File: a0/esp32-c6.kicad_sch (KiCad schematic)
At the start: 11 parts, among them J1 Conn_ARM_JTAG_SWD_10, SW1 SW_Push, SW2 SW_Push, U1 ESP32-C6-MINI-1/U

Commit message: update A0
Signed-off-by: Rodney Osodo <socials@rodneyosodo.com>
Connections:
- net USB_D+: now also U1.18 (GPIO13/USB_D+); no longer U1.17 (GPIO12/USB_D-)
- net USB_D-: now also U1.17 (GPIO12/USB_D-); no longer U1.18 (GPIO13/USB_D+)
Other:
- note added: "ESP32C6"
- note added: "JTAG"
- note added: "PULL UP"
- company: (none) -> Abstract Machines
- title: (none) -> A0
- moved on the sheet: C1, C2, C3, C4, J1, R1, R2, R3, SW1, SW2, U1

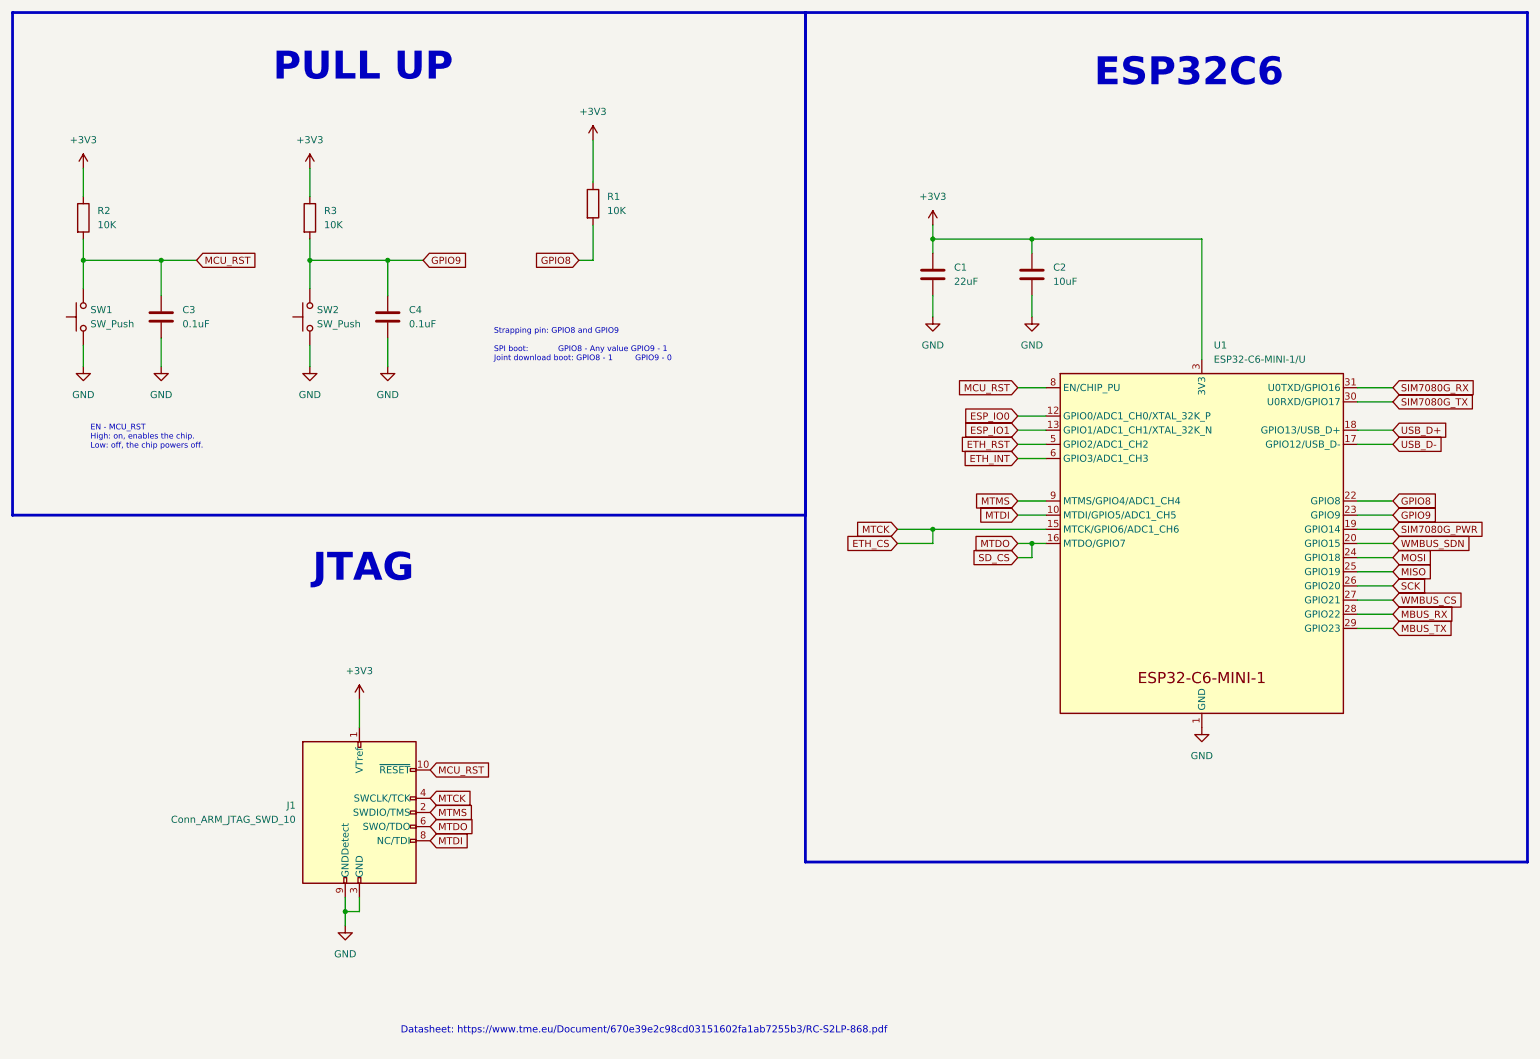
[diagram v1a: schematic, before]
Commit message: fix(A0): update to use modules
Signed-off-by: Rodney Osodo <socials@rodneyosodo.com>
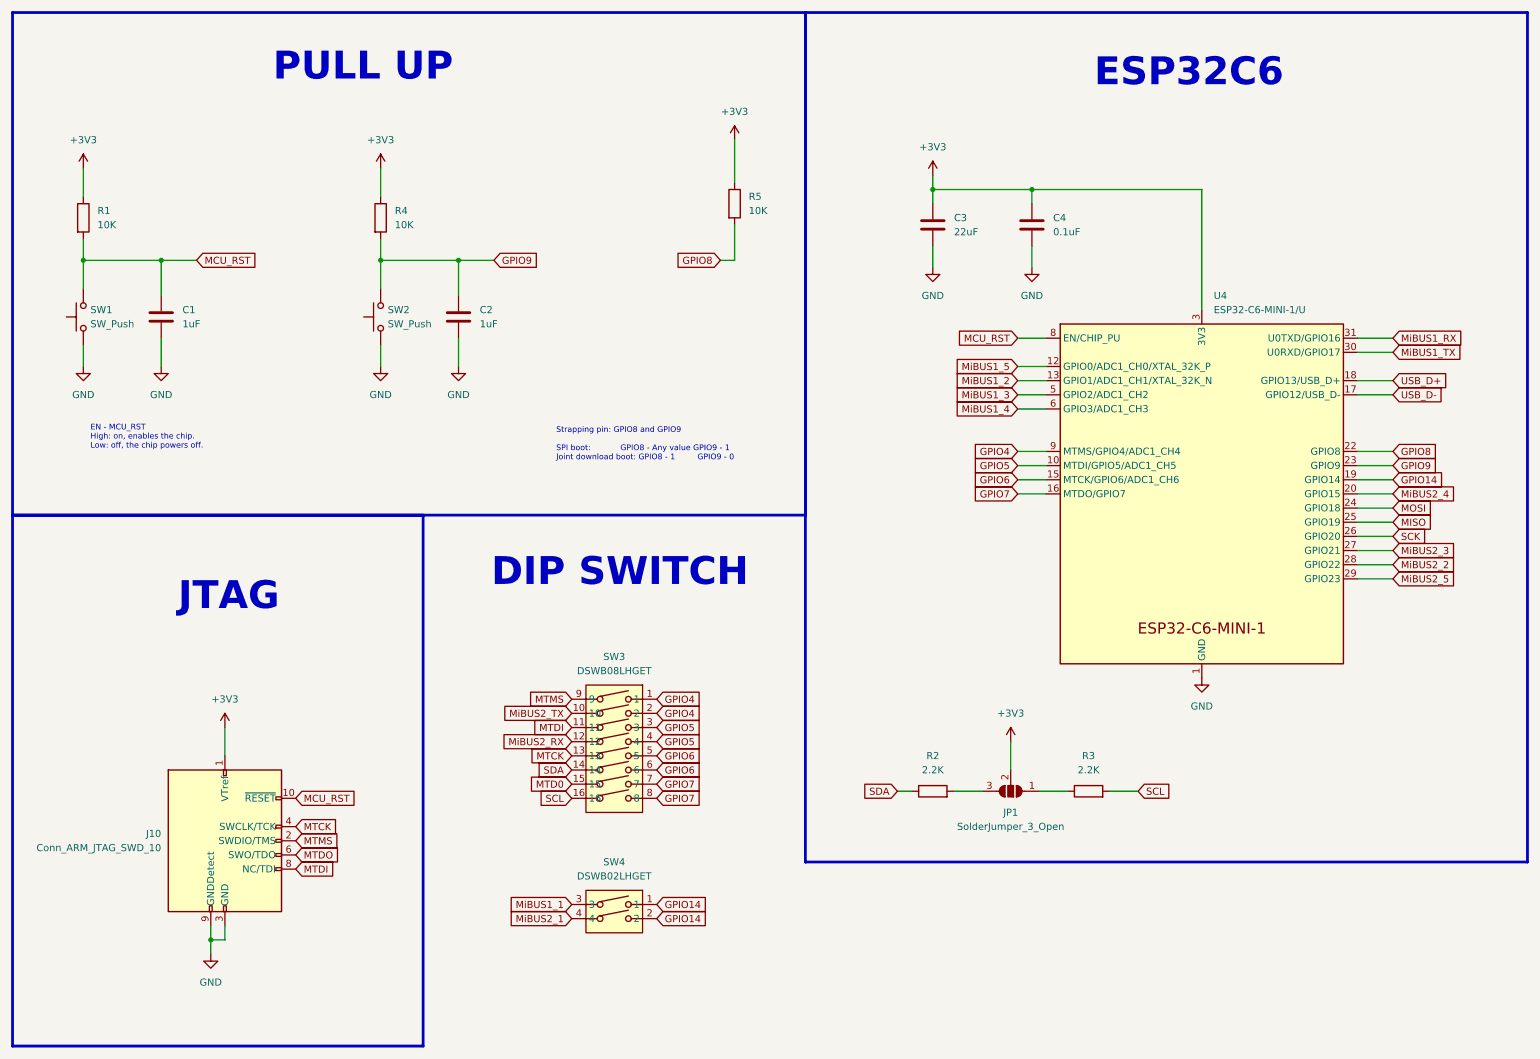
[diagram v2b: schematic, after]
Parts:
- removed J1: Conn_ARM_JTAG_SWD_10, Connector_PinHeader_1.27mm:PinHeader_2x05_P1.27mm_Vertical, symbol Connector:Conn_ARM_JTAG_SWD_10
- added J10: Conn_ARM_JTAG_SWD_10, Connector_PinHeader_1.27mm:PinHeader_2x05_P1.27mm_Vertical, symbol Connector:Conn_ARM_JTAG_SWD_10
- added JP1: SolderJumper_3_Open, Jumper:SolderJumper-3_P1.3mm_Open_RoundedPad1.0x1.5mm, symbol Jumper:SolderJumper_3_Open
- added R2, R3: 2.2K, Resistor_SMD:R_0805_2012Metric, symbol Device:R
- added SW3: DSWB08LHGET, modules:C99413, symbol C99413:DSWB08LHGET
- added SW4: DSWB02LHGET, modules:C99421, symbol C99421:DSWB02LHGET
- C1: renamed from C3; value 0.1uF -> 1uF; JLCPCB C49678 -> C28323
- C2: renamed from C4; value 0.1uF -> 1uF; JLCPCB C49678 -> C28323
- C4: renamed from C2; value 10uF -> 0.1uF; JLCPCB C15850 -> C49678
- renumbered C1 to C3, R2 to R1, R3 to R4, R1 to R5, U1 to U4
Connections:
- net +3V3: now also J10.1 (VTref), JP1.2 (C)
- net GND: now also J10.3 (GND), J10.5 (GND), J10.9 (GNDDetect)
- net MCU_RST: now also J10.10 (~{RESET})
- net MTDI: now also J10.8 (NC/TDI), SW3.11; no longer U4.10 (MTDI/GPIO5/ADC1_CH5)
- net MTDO: now also J10.6 (SWO/TDO); no longer U4.16 (MTDO/GPIO7)
- net MTMS: now also J10.2 (SWDIO/TMS), SW3.9; no longer U4.9 (MTMS/GPIO4/ADC1_CH4)
- net ESP_IO0 renamed MiBUS1_5
- net ESP_IO1 renamed MiBUS1_2
- net ETH_CS renamed GPIO6
- net GPIO6: now also SW3.5, SW3.6
- net ETH_INT renamed MiBUS1_4
- net ETH_RST renamed MiBUS1_3
- net MBUS_RX renamed MiBUS2_2
- net MBUS_TX renamed MiBUS2_5
- net SIM7080G_PWR renamed GPIO14
- net GPIO14: now also SW4.1, SW4.2
- net SIM7080G_RX renamed MiBUS1_RX
- net SIM7080G_TX renamed MiBUS1_TX
- net WMBUS_CS renamed MiBUS2_3
- net WMBUS_SDN renamed MiBUS2_4
- new net: JP1.3 (B), R2.2
- new net: JP1.1 (A), R3.1
- new net GPIO4: SW3.1, SW3.2, U4.9 (MTMS/GPIO4/ADC1_CH4)
- new net GPIO5: SW3.3, SW3.4, U4.10 (MTDI/GPIO5/ADC1_CH5)
- new net GPIO7: SW3.7, SW3.8, U4.16 (MTDO/GPIO7)
- new net MTCK: J10.4 (SWCLK/TCK), SW3.13
- new net MTD0: SW3.15
- new net MiBUS1_1: SW4.3
- new net MiBUS2_1: SW4.4
- new net MiBUS2_RX: SW3.12
- new net MiBUS2_TX: SW3.10
- new net SCL: R3.2, SW3.16
- new net SDA: R2.1, SW3.14
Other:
- note added: "DIP SWITCH"
- note removed: "Datasheet: https://www.tme.eu/Document/670e39e2c98cd03151602fa1ab7255b3/RC-S2LP-868.pdf"
- moved on the sheet: C2, C3, C4, R4, R5, SW2, U4

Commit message: feat: update A0
Signed-off-by: Rodney Osodo <socials@rodneyosodo.com>
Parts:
- removed SW3: DSWB08LHGET, modules:C99413, symbol C99413:DSWB08LHGET
- removed SW4: DSWB02LHGET, modules:C99421, symbol C99421:DSWB02LHGET
- added SW5: SMXS-08K-TP, modules:C5439767, symbol C5439767:SMXS-08K-TP
- added U1: SMXS-02K-TP, modules:C5439761, symbol C5439761:SMXS-02K-TP
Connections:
- net GPIO14: now also U1.1, U1.2
- net GPIO4: now also SW5.7, SW5.8
- net GPIO5: now also SW5.5, SW5.6
- net GPIO6: now also SW5.3, SW5.4
- net GPIO7: now also SW5.1, SW5.2
- net MTCK: now also SW5.13
- net MTD0: now also SW5.15
- net MTDI: now also SW5.11
- net MTMS: now also SW5.9
- net MiBUS1_1: now also U1.3
- net MiBUS2_1: now also U1.4
- net MiBUS2_RX: now also SW5.12
- net MiBUS2_TX: now also SW5.10
- net SCL: now also SW5.16
- net SDA: now also SW5.14
